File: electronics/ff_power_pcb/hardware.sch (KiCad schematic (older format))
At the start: 56 parts, among them U3 TPS62095RGTR, U4 TPS62095RGTR, U5 TPS62095RGTR, U6 TPS62095RGTR, U7 AP131-25

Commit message: Roughed in the transformer and whatnot.
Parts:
- added C1: 22uF, Capacitor_SMD:C_0805_2012Metric, symbol Device:C_Small
- added D1, D2, D3, D4: D, symbol Device:D
- added J1, J2: Conn_01x01_Female, symbol Connector:Conn_01x01_Female
- added T1: Transformer_1P_1S, symbol Device:Transformer_1P_1S
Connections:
- wire segments 260 -> 282
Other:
- note added: "120:24"
- note added: "120VAC"
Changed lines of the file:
@@
 Connection ~ 9300 9250
 Connection ~ 7900 9250
+$Comp
+L Device:Transformer_1P_1S T1
+U 1 1 60C2D30D
+P 3000 1800
+F 0 "T1" H 3000 2089 50  0000 C CNN
+F 1 "Transformer_1P_1S" H 3000 2090 50  0001 C CNN
+F 2 "" H 3000 1800 50  0001 C CNN
+F 3 "~" H 3000 1800 50  0001 C CNN
+	1    3000 1800
+	1    0    0    -1
+$EndComp
+Text Notes 2800 2200 0    79   ~ 0
+120:24
+$Comp
+L Connector:Conn_01x01_Female J1
+U 1 1 60C35847
+P 1800 1600
+F 0 "J1" H 1692 1467 50  0000 C CNN
+F 1 "Conn_01x01_Female" H 1692 1466 50  0001 C CNN
+F 2 "" H 1800 1600 50  0001 C CNN
+F 3 "~" H 1800 1600 50  0001 C CNN
+	1    1800 1600
+	-1   0    0    1
+$EndComp
+Wire Wire Line
+	2000 1600 2600 1600
+$Comp
+L Connector:Conn_01x01_Female J2
+U 1 1 60C45FDE
+P 1800 2000
+F 0 "J2" H 1692 1867 50  0000 C CNN
+F 1 "Conn_01x01_Female" H 1692 1866 50  0001 C CNN
+F 2 "" H 1800 2000 50  0001 C CNN
+F 3 "~" H 1800 2000 50  0001 C CNN
+	1    1800 2000
+	-1   0    0    1
+$EndComp
+Wire Wire Line
+	2000 2000 2600 2000
+Text Notes 1300 1850 0    79   ~ 0
+120VAC
+$Comp
+L Device:D D1
+U 1 1 60C685EC
+P 3950 1300
+F 0 "D1" V 3904 1380 50  0000 L CNN
+F 1 "D" V 3995 1380 50  0000 L CNN
+F 2 "" H 3950 1300 50  0001 C CNN
+F 3 "~" H 3950 1300 50  0001 C CNN
+	1    3950 1300
+	0    1    1    0
+$EndComp
+$Comp
+L Device:D D3
+U 1 1 60C79052
+P 4650 1300
+F 0 "D3" V 4604 1380 50  0000 L CNN
+F 1 "D" V 4695 1380 50  0000 L CNN
+F 2 "" H 4650 1300 50  0001 C CNN
+F 3 "~" H 4650 1300 50  0001 C CNN
+	1    4650 1300
+	0    1    1    0
+$EndComp
+$Comp
+L Device:D D4
+U 1 1 60C79367
+P 3950 2200
+F 0 "D4" V 3904 2280 50  0000 L CNN
+F 1 "D" V 3995 2280 50  0000 L CNN
+F 2 "" H 3950 2200 50  0001 C CNN
+F 3 "~" H 3950 2200 50  0001 C CNN
+	1    3950 2200
+	0    1    1    0
+$EndComp
+$Comp
+L Device:D D2
+U 1 1 60C796F5
+P 4650 2200
+F 0 "D2" V 4604 2280 50  0000 L CNN
+F 1 "D" V 4695 2280 50  0000 L CNN
+F 2 "" H 4650 2200 50  0001 C CNN
+F 3 "~" H 4650 2200 50  0001 C CNN
+	1    4650 2200
+	0    1    1    0
+$EndComp
+Wire Wire Line
+	3950 1450 3950 1600
+Wire Wire Line
+	4650 1450 4650 2000
+Wire Wire Line
+	3400 1600 3950 1600
+Connection ~ 3950 1600
+Wire Wire Line
+	3950 1600 3950 2050
+Wire Wire Line
+	3400 2000 4650 2000
+Connection ~ 4650 2000
+Wire Wire Line
+	4650 2000 4650 2050
+Wire Wire Line
+	3950 2350 3950 2450
+Wire Wire Line
+	4650 2350 4650 2450
+Connection ~ 4650 2450
+Wire Wire Line
+	3950 1150 3950 1050
+Wire Wire Line
+	4650 1150 4650 1050
+Connection ~ 4650 1050
+$Comp
+L power:GND #PWR02
+U 1 1 60DA36BC
+P 5000 2600
+F 0 "#PWR02" H 5000 2350 50  0001 C CNN
+F 1 "GND" H 5005 2427 50  0000 C CNN
+F 2 "" H 5000 2600 50  0001 C CNN
+F 3 "" H 5000 2600 50  0001 C CNN
+	1    5000 2600
+	1    0    0    -1
+$EndComp
+Wire Wire Line
+	5000 2600 5000 2450
+Connection ~ 5000 2450
+Wire Wire Line
+	5000 2450 5350 2450
+$Comp
+L Device:C_Small C?
+U 1 1 60DB8801
+P 5350 1700
+AR Path="/60536DA4/60DB8801" Ref="C?"  Part="1"
+AR Path="/60A30BFF/60DB8801" Ref="C?"  Part="1"
+AR Path="/60DB8801" Ref="C1"  Part="1"
+F 0 "C1" H 5400 1800 50  0000 L CNN
+F 1 "22uF" H 5400 1600 50  0000 L CNN
+F 2 "Capacitor_SMD:C_0805_2012Metric" H 5350 1700 50  0001 C CNN
+F 3 "~" H 5350 1700 50  0001 C CNN
+F 4 "CL21A226MQQNNNE" H 5400 1900 50  0001 C CNN "MPN"
+F 5 "~" H 5400 1900 50  0001 C CNN "Tolerance"
+	1    5350 1700
+	1    0    0    -1
+$EndComp
+Wire Wire Line
+	5350 1600 5350 1050
+Wire Wire Line
+	5350 1800 5350 2450
+Wire Wire Line
+	4650 1050 5000 1050
+$Comp
+L power:+5V #PWR01
+U 1 1 60E0A16B
+P 5000 950
+F 0 "#PWR01" H 5000 800 50  0001 C CNN
+F 1 "+5V" H 5015 1123 50  0000 C CNN
+F 2 "" H 5000 950 50  0001 C CNN
+F 3 "" H 5000 950 50  0001 C CNN
+	1    5000 950
+	1    0    0    -1
+$EndComp
+Wire Wire Line
+	5000 1050 5000 950
+Wire Wire Line
+	4650 2450 5000 2450
+Wire Wire Line
+	3950 1050 4650 1050
+Wire Wire Line
+	3950 2450 4650 2450
+Connection ~ 5000 1050
+Wire Wire Line
+	5000 1050 5350 1050
 $EndSCHEMATC

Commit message: Just made some notes, added apower budget.
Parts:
- added D5: D_TVS, symbol Device:D_TVS
- added F1: Fuse, symbol Device:Fuse
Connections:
- wire segments 282 -> 287
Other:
- moved on the sheet: J1, J2
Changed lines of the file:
@@
 encoding utf-8
 Sheet 1 1
-Title "Wifi Ward - FF Power Board"
+Title "Wifi Wart - FF Power Board"
 Date ""
 Rev "R0.1"
@@
 L Connector:Conn_01x01_Female J1
 U 1 1 60C35847
-P 1800 1600
-F 0 "J1" H 1692 1467 50  0000 C CNN
-F 1 "Conn_01x01_Female" H 1692 1466 50  0001 C CNN
-F 2 "" H 1800 1600 50  0001 C CNN
-F 3 "~" H 1800 1600 50  0001 C CNN
-	1    1800 1600
+P 1250 1600
+F 0 "J1" H 1142 1467 50  0000 C CNN
+F 1 "Conn_01x01_Female" H 1142 1466 50  0001 C CNN
+F 2 "" H 1250 1600 50  0001 C CNN
+F 3 "~" H 1250 1600 50  0001 C CNN
+	1    1250 1600
 	-1   0    0    1
 $EndComp
 Wire Wire Line
-	2000 1600 2600 1600
+	1450 1600 1600 1600
 $Comp
 L Connector:Conn_01x01_Female J2
 U 1 1 60C45FDE
-P 1800 2000
-F 0 "J2" H 1692 1867 50  0000 C CNN
-F 1 "Conn_01x01_Female" H 1692 1866 50  0001 C CNN
-F 2 "" H 1800 2000 50  0001 C CNN
-F 3 "~" H 1800 2000 50  0001 C CNN
-	1    1800 2000
+P 1250 2000
+F 0 "J2" H 1142 1867 50  0000 C CNN
+F 1 "Conn_01x01_Female" H 1142 1866 50  0001 C CNN
+F 2 "" H 1250 2000 50  0001 C CNN
+F 3 "~" H 1250 2000 50  0001 C CNN
+	1    1250 2000
 	-1   0    0    1
 $EndComp
 Wire Wire Line
-	2000 2000 2600 2000
-Text Notes 1300 1850 0    79   ~ 0
+	1450 2000 2200 2000
+Text Notes 750  1850 0    79   ~ 0
 120VAC
 $Comp
@@
 Wire Wire Line
 	5000 1050 5350 1050
+$Comp
+L Device:Fuse F1
+U 1 1 60B49BE3
+P 1750 1600
+F 0 "F1" V 1553 1600 50  0000 C CNN
+F 1 "Fuse" V 1644 1600 50  0000 C CNN
+F 2 "" V 1680 1600 50  0001 C CNN
+F 3 "~" H 1750 1600 50  0001 C CNN
+	1    1750 1600
+	0    1    1    0
+$EndComp
+Wire Wire Line
+	1900 1600 2200 1600
+$Comp
+L Device:D_TVS D5
+U 1 1 60B65CEC
+P 2200 1800
+F 0 "D5" V 2154 1880 50  0000 L CNN
+F 1 "D_TVS" V 2245 1880 50  0000 L CNN
+F 2 "" H 2200 1800 50  0001 C CNN
+F 3 "~" H 2200 1800 50  0001 C CNN
+	1    2200 1800
+	0    1    1    0
+$EndComp
+Wire Wire Line
+	2200 1650 2200 1600
+Connection ~ 2200 1600
+Wire Wire Line
+	2200 1600 2600 1600
+Wire Wire Line
+	2200 1950 2200 2000
+Connection ~ 2200 2000
+Wire Wire Line
+	2200 2000 2600 2000
 $EndSCHEMATC

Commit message: Dopped all the parts down for the power supply.
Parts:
- removed D1, D2, D3, D4: D, symbol Device:D
- removed D5: D_TVS, symbol Device:D_TVS
- removed J1, J2: Conn_01x01_Female, symbol Connector:Conn_01x01_Female
- removed T1: Transformer_1P_1S, symbol Device:Transformer_1P_1S
- added C2: 33uF, Capacitor_SMD:C_0805_2012Metric, symbol Device:C_Small
- added C29: 0.1uF, symbol Device:C_Small
- added C3: 2.2nF, symbol Device:C_Small
- added C4: 470uF, Capacitor_SMD:C_0805_2012Metric, symbol Device:C_Small
- added C5: 220uF, Capacitor_SMD:C_0805_2012Metric, symbol Device:C_Small
- added D1: D_Zener, symbol Device:D_Zener
- added L5: 1.2mH, symbol Device:L
- added L6: 2.2uF, symbol Device:L
- added PS1: PBO-15C-5, CUI:CONV_PBO-15C-5, symbol CUI:PBO-15C-5
- added TH1: Thermistor_NTC, symbol Device:Thermistor_NTC
- C1: value 22uF -> 0.1uF; footprint Capacitor_SMD:C_0805_2012Metric -> (none); MPN CL21A226MQQNNNE -> (none); Voltage (none) -> 310V
- F1: value Fuse -> 1A/300V Slow
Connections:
- net labels added: AC_L, AC_N
- wire segments 287 -> 303
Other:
- note added: "85-305Vac"
- note removed: "120:24"
- note removed: "120VAC"

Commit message: Added an app note of ntc current limiting, and added some part numbers into the schematic.
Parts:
- C1: footprint (none) -> Capacitor_SMD:C_1206_3216Metric; MPN (none) -> C3216X7T2V104M160AA
- C29: footprint (none) -> Capacitor_SMD:C_0603_1608Metric; MPN (none) -> C1608X7R1H104K080AA
- C4, C5: footprint Capacitor_SMD:C_0805_2012Metric -> (none)
- F1: footprint (none) -> Fuse:Fuse_Littelfuse-NANO2-451_453; MPN (none) -> 0679H1000-01
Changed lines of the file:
@@
 F 0 "C1" H 6450 2300 50  0000 L CNN
 F 1 "0.1uF" H 6450 2100 50  0000 L CNN
-F 2 "" H 6400 2200 50  0001 C CNN
+F 2 "Capacitor_SMD:C_1206_3216Metric" H 6400 2200 50  0001 C CNN
 F 3 "~" H 6400 2200 50  0001 C CNN
-F 4 "" H 6450 2400 50  0001 C CNN "MPN"
+F 4 "C3216X7T2V104M160AA" H 6450 2400 50  0001 C CNN "MPN"
 F 5 "~" H 6450 2400 50  0001 C CNN "Tolerance"
 F 6 "310V" H 6550 2000 50  0000 C CNN "Voltage"
@@
 F 0 "F1" V 5153 1900 50  0000 C CNN
 F 1 "1A/300V Slow" V 5244 1900 50  0000 C CNN
-F 2 "" V 5280 1900 50  0001 C CNN
+F 2 "Fuse:Fuse_Littelfuse-NANO2-451_453" V 5280 1900 50  0001 C CNN
 F 3 "~" H 5350 1900 50  0001 C CNN
+F 4 "0679H1000-01" V 5350 1900 50  0001 C CNN "MPN"
 	1    5350 1900
 	0    1    1    0
@@
 F 0 "C4" H 9050 2300 50  0000 L CNN
 F 1 "470uF" H 9050 2100 50  0000 L CNN
-F 2 "Capacitor_SMD:C_0805_2012Metric" H 9000 2200 50  0001 C CNN
+F 2 "" H 9000 2200 50  0001 C CNN
 F 3 "~" H 9000 2200 50  0001 C CNN
 F 4 "" H 9050 2400 50  0001 C CNN "MPN"
@@
 F 0 "C5" H 9650 2300 50  0000 L CNN
 F 1 "220uF" H 9650 2100 50  0000 L CNN
-F 2 "Capacitor_SMD:C_0805_2012Metric" H 9600 2200 50  0001 C CNN
+F 2 "" H 9600 2200 50  0001 C CNN
 F 3 "~" H 9600 2200 50  0001 C CNN
 F 4 "" H 9650 2400 50  0001 C CNN "MPN"
@@
 F 0 "C29" H 10750 2300 50  0000 L CNN
 F 1 "0.1uF" H 10750 2100 50  0000 L CNN
-F 2 "" H 10700 2200 50  0001 C CNN
+F 2 "Capacitor_SMD:C_0603_1608Metric" H 10700 2200 50  0001 C CNN
 F 3 "~" H 10700 2200 50  0001 C CNN
-F 4 "" H 10750 2400 50  0001 C CNN "MPN"
+F 4 "C1608X7R1H104K080AA" H 10750 2400 50  0001 C CNN "MPN"
 F 5 "~" H 10750 2400 50  0001 C CNN "Tolerance"
 F 6 "50V" H 10850 2000 50  0000 C CNN "Voltage"

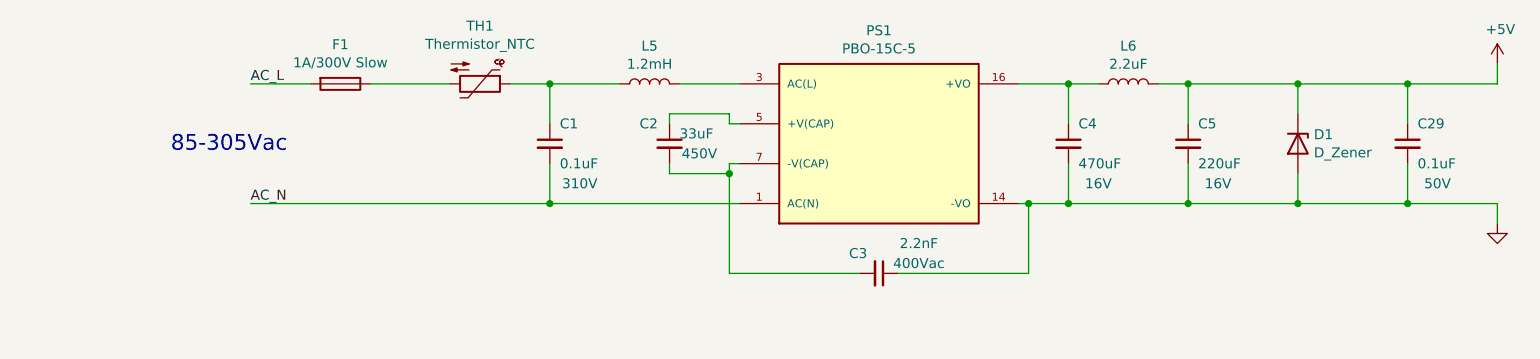
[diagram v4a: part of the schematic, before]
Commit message: Dropping the parts into the layout.
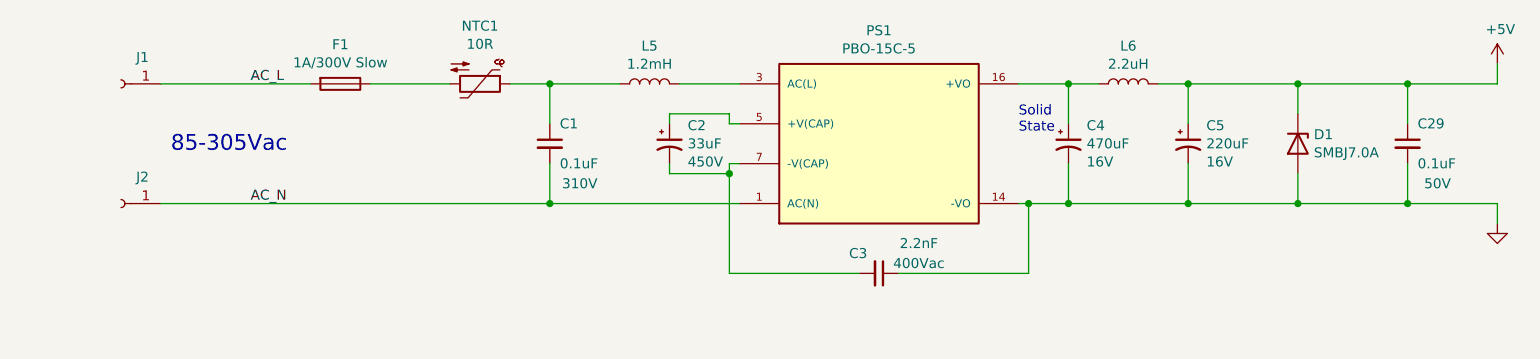
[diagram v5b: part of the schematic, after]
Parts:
- removed C2: 33uF, Capacitor_SMD:C_0805_2012Metric, symbol Device:C_Small
- removed C4: 470uF, symbol Device:C_Small
- removed C5: 220uF, symbol Device:C_Small
- added C2: 33uF, Capacitor_THT:C_Radial_D16.0mm_H25.0mm_P7.50mm, symbol Device:CP1_Small
- added C4: 470uF, Capacitor_SMD:CP_Elec_10x12.5, symbol Device:CP1_Small
- added C5: 220uF, Capacitor_SMD:CP_Elec_8x10.5, symbol Device:CP1_Small
- added J1, J2: Conn_01x01_Female, Connector_PinHeader_2.54mm:PinHeader_1x01_P2.54mm_Vertical, symbol Connector:Conn_01x01_Female
- C3: footprint (none) -> Capacitor_SMD:C_1206_3216Metric; MPN (none) -> 501R18W223KV4E
- D1: value D_Zener -> SMBJ7.0A; footprint (none) -> Diode_SMD:D_SMB; MPN (none) -> SMBJ7.0A
- L5: MPN (none) -> SRR1208-122KL
- L6: value 2.2uF -> 2.2uH; footprint (none) -> Inductor_SMD:L_Coilcraft_XxL4020; MPN (none) -> XAL4020-222ME
- NTC1: renamed from TH1; value Thermistor_NTC -> 10R; footprint (none) -> Capacitor_THT:C_Disc_D9.0mm_W2.5mm_P5.00mm
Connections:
- net +5V: now also C5.1
- net AC_L: now also J1.1 (Pin_1)
- net AC_N: now also J2.1 (Pin_1)
- net GND: now also C4.2, C5.2
- net at L6.1, PS1.16 (+VO): now also C4.1
- net at PS1.5 (+V(CAP)): now also C2.1
- net at C3.2, PS1.7 (-V(CAP)): now also C2.2
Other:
- note added: "Solid\nState"

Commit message: All footprints are in.
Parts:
- L5: footprint (none) -> Bourns:RLB9012; MPN SRR1208-122KL -> RLB9012-122KL
- NTC1: MPN (none) -> B57234S0100M051
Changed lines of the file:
@@
 F 2 "Capacitor_THT:C_Disc_D9.0mm_W2.5mm_P5.00mm" H 6050 1950 50  0001 C CNN
 F 3 "~" H 6050 1950 50  0001 C CNN
+F 4 "B57234S0100M051" V 6050 1900 50  0001 C CNN "MPN"
 	1    6050 1900
 	0    1    1    0
@@
 F 0 "L5" V 7090 1900 50  0000 C CNN
 F 1 "1.2mH" V 6999 1900 50  0000 C CNN
-F 2 "" H 6900 1900 50  0001 C CNN
+F 2 "Bourns:RLB9012" H 6900 1900 50  0001 C CNN
 F 3 "~" H 6900 1900 50  0001 C CNN
-F 4 "SRR1208-122KL" V 6900 1900 50  0001 C CNN "MPN"
+F 4 "RLB9012-122KL" V 6900 1900 50  0001 C CNN "MPN"
 	1    6900 1900
 	0    -1   -1   0
